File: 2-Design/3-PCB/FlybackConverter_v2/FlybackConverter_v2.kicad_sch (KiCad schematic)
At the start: 55 parts, among them U1 TL431DBZ, U2 LM7812_TO220

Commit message: Gate loop is not long anymore. Still, why not be sad :(.
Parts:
- CA1: value C -> 1n
- CF1: value C -> 20p
- CP1: value C -> NAN
- CS1: value C -> 10n
- CSnubber1: value C -> 4.7u-2220-50V
- CT1: value C -> 0.72n
- CZ1: value C -> 20n
- DSnubber1: value MBRA340 -> M3/5BT; footprint Diode_SMD:D_SMA -> Diode_SMD:D_SMB_Handsoldering
- FLYBACK_DIODE_SUBSTITUTE1: footprint Diode_SMD:D_SMC -> Diode_SMD:D_SMC_Handsoldering
- RA1, RF1, RJ1, RP1: value R -> 10k
- RAC1, RE1: value R -> 1k
- RB1, RC1, RK1: value R -> 4.7k
- RCS1: value R -> 10m
- RG1: value R -> 10
- RG2, RZ1: value R -> 22k
- RI1: value R -> 85k
- RS1: value R -> 330k
- RS2: value R -> 2.2k
- RSnubber1: value R -> 82//82
- RT1: value 10 -> 12k
- renumbered DC1 to D_Z_10V1, TVS1 to D_Z_15V1
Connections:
- net GND: now also RG2.1
- net at MOSFET1.1 (S), RCS1.1, RS2.2: no longer RG2.1
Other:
- moved on the sheet: RA1

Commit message: [PCB] board update
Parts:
- added CSnubber2: 4.7u-2220-50V, Capacitor_SMD:C_1210_3225Metric_Pad1.33x2.70mm_HandSolder, symbol Device:C
- added RG3: 0, Resistor_SMD:R_1206_3216Metric, symbol Device:R
- added RSnubber2: 82//82, Resistor_SMD:R_2010_5025Metric_Pad1.40x2.65mm_HandSolder, symbol Device:R
- CF1: value 20p -> 22p
- CZ1: value 20n -> 22n
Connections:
- net at CIN1.1, CIN2.1, CIN3.1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: now also CSnubber2.1, RG3.2, RSnubber2.1; no longer U2.1 (VI)
- net at CSnubber1.2, DSnubber1.1 (K), RSnubber1.2: now also CSnubber2.2, RSnubber2.2
- new net: RG3.1, U2.1 (VI)
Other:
- note added: "TO DO - heatsink model [DONE] - transformer model[DONE] - connector size check [DONE] - optpcoupler freq check [DONE] - current sense check (sim, iranian resistor) [DONE] - components layer check [DONE] - via check [DONE] - plexi case"
- note removed: "TO DO - heatsink model - transformer model - connector size check - optpcoupler freq check - current sense check (sim, iranian resistor) - components layer check - via check - plexi case"
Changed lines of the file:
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@@
 (kicad_sch (version 20211123) (generator eeschema)
   (paper "A4")
+  (junction (at 173.99 38.1) (diameter 0) (color 0 0 0 0)
+  )
   (junction (at 100.33 72.39) (diameter 0) (color 0 0 0 0)
   )
@@
   (junction (at 105.41 38.1) (diameter 0) (color 0 0 0 0)
   )
+  (junction (at 171.45 49.53) (diameter 0) (color 0 0 0 0)
+  )
   (junction (at 154.94 128.27) (diameter 0) (color 0 0 0 0)
   )
@@
   (junction (at 180.34 86.36) (diameter 0) (color 0 0 0 0)
   )
+  (junction (at 171.45 38.1) (diameter 0) (color 0 0 0 0)
+  )
   (junction (at 87.63 62.23) (diameter 0) (color 0 0 0 0)
   )
@@
   (junction (at 224.79 44.45) (diameter 0) (color 0 0 0 0)
   )
+  (junction (at 173.99 49.53) (diameter 0) (color 0 0 0 0)
+  )
   (junction (at 97.79 74.93) (diameter 0) (color 0 0 0 0)
   )
@@
   (junction (at 64.77 62.23) (diameter 0) (color 0 0 0 0)
   )
-  (wire (pts (xy 147.32 57.15) (xy 161.29 57.15))
+  (wire (pts (xy 147.32 57.15) (xy 148.59 57.15))
     (stroke (width 0) (type default) (color 0 0 0 0))
   )
@@
     (stroke (width 0) (type default) (color 0 0 0 0))
   )
+  (wire (pts (xy 156.21 57.15) (xy 161.29 57.15))
+    (stroke (width 0) (type default) (color 0 0 0 0))
+  )
   (wire (pts (xy 115.57 55.88) (xy 129.54 55.88))
     (stroke (width 0) (type default) (color 0 0 0 0))
@@
     (stroke (width 0) (type default) (color 0 0 0 0))
   )
+  (wire (pts (xy 171.45 38.1) (xy 171.45 40.64))
+    (stroke (width 0) (type default) (color 0 0 0 0))
+  )
   (wire (pts (xy 172.72 86.36) (xy 180.34 86.36))
     (stroke (width 0) (type default) (color 0 0 0 0))
   )
+  (wire (pts (xy 173.99 49.53) (xy 171.45 49.53))
+    (stroke (width 0) (type default) (color 0 0 0 0))
+  )
   (wire (pts (xy 153.67 87.63) (xy 153.67 88.9))
     (stroke (width 0) (type default) (color 0 0 0 0))
@@
     (stroke (width 0) (type default) (color 0 0 0 0))
   )
-  (wire (pts (xy 176.53 49.53) (xy 170.18 49.53))
+  (wire (pts (xy 176.53 49.53) (xy 173.99 49.53))
     (stroke (width 0) (type default) (color 0 0 0 0))
   )
@@
     (stroke (width 0) (type default) (color 0 0 0 0))
   )
+  (wire (pts (xy 173.99 38.1) (xy 173.99 40.64))
+    (stroke (width 0) (type default) (color 0 0 0 0))
+  )
   (wire (pts (xy 147.32 116.84) (xy 147.32 111.76))
     (stroke (width 0) (type default) (color 0 0 0 0))
@@
     (stroke (width 0) (type default) (color 0 0 0 0))
   )
+  (wire (pts (xy 173.99 38.1) (xy 176.53 38.1))
+    (stroke (width 0) (type default) (color 0 0 0 0))
+  )
+  (wire (pts (xy 171.45 49.53) (xy 170.18 49.53))
+    (stroke (width 0) (type default) (color 0 0 0 0))
+  )
   (wire (pts (xy 167.64 60.96) (xy 167.64 78.74))
     (stroke (width 0) (type default) (color 0 0 0 0))
@@
     (stroke (width 0) (type default) (color 0 0 0 0))
   )
+  (wire (pts (xy 171.45 48.26) (xy 171.45 49.53))
+    (stroke (width 0) (type default) (color 0 0 0 0))
+  )
+  (wire (pts (xy 173.99 48.26) (xy 173.99 49.53))
+    (stroke (width 0) (type default) (color 0 0 0 0))
+  )
   (wire (pts (xy 176.53 48.26) (xy 176.53 49.53))
     (stroke (width 0) (type default) (color 0 0 0 0))
@@
     (stroke (width 0) (type default) (color 0 0 0 0))
   )
-  (wire (pts (xy 166.37 38.1) (xy 176.53 38.1))
+  (wire (pts (xy 166.37 38.1) (xy 171.45 38.1))
     (stroke (width 0) (type default) (color 0 0 0 0))
   )
@@
     (stroke (width 0) (type default) (color 0 0 0 0))
   )
+  (wire (pts (xy 171.45 38.1) (xy 173.99 38.1))
+    (stroke (width 0) (type default) (color 0 0 0 0))
+  )
   (wire (pts (xy 165.1 64.77) (xy 172.72 64.77))
     (stroke (width 0) (type default) (color 0 0 0 0))
@@
     (stroke (width 0) (type default) (color 0 0 0 0))
   )
-  (text "TO DO\n- heatsink model\n- transformer model\n- connector size check\n- optpcoupler freq check\n- current sense check (sim, iranian resistor)\n- components layer check\n- via check\n- plexi case\n"
+  (text "TO DO\n- heatsink model [DONE]\n- transformer model[DONE]\n- connector size check [DONE]\n- optpcoupler freq check [DONE]\n- current sense check (sim, iranian resistor) [DONE]\n- components layer check [DONE]\n- via check [DONE]\n- plexi case\n"
     (at 13.97 34.29 0)
     (effects (font (size 1.27 1.27)) (justify left bottom))
@@
     (pin "1")
   )
+  (symbol (lib_id "Device:R") (at 152.4 57.15 90) (unit 1)
+    (in_bom yes) (on_board yes)
+    (property "Reference" "RG3" (id 0) (at 152.4 52.07 90))
+    (property "Value" "0" (id 1) (at 152.4 54.61 90))
+    (property "Footprint" "Resistor_SMD:R_1206_3216Metric" (id 2) (at 152.4 58.928 90)
+      (effects (font (size 1.27 1.27)) hide)
+    )
+    (property "Datasheet" "~" (id 3) (at 152.4 57.15 0)
+      (effects (font (size 1.27 1.27)) hide)
+    )
+    (pin "1")
+    (pin "2")
+  )
   (symbol (lib_id "Device:C") (at 76.2 55.88 90) (unit 1)
     (in_bom yes) (on_board yes)
@@
     (in_bom yes) (on_board yes)
     (property "Reference" "CZ1" (id 0) (at 170.18 116.84 90))
-    (property "Value" "20n" (id 1) (at 170.18 119.38 90))
+    (property "Value" "22n" (id 1) (at 170.18 119.38 90))
     (property "Footprint" "Capacitor_SMD:C_0805_2012Metric_Pad1.18x1.45mm_HandSolder" (id 2) (at 173.99 122.2248 0)
       (effects (font (size 1.27 1.27)) hide)
@@
     (pin "2")
   )
+  (symbol (lib_id "Device:R") (at 173.99 44.45 0) (unit 1)
+    (in_bom yes) (on_board yes)
+    (property "Reference" "RSnubber2" (id 0) (at 171.45 34.29 0)
+      (effects (font (size 1.27 1.27)) (justify left))
+    )
+    (property "Value" "82//82" (id 1) (at 172.72 36.83 0)
+      (effects (font (size 1.27 1.27)) (justify left))
+    )
+    (property "Footprint" "Resistor_SMD:R_2010_5025Metric_Pad1.40x2.65mm_HandSolder" (id 2) (at 172.212 44.45 90)
+      (effects (font (size 1.27 1.27)) hide)
+    )
+    (property "Datasheet" "~" (id 3) (at 173.99 44.45 0)
+      (effects (font (size 1.27 1.27)) hide)
+    )
+    (pin "1")
+    (pin "2")
+  )
   (symbol (lib_id "Reference_Voltage:TL431DBZ") (at 147.32 128.27 270) (mirror x) (unit 1)
     (in_bom yes) (on_board yes) (fields_autoplaced)
@@
       (effects (font (size 1.27 1.27)) (justify left))
     )
-    (property "Value" "20p" (id 1) (at 157.48 81.2799 0)
+    (property "Value" "22p" (id 1) (at 157.48 81.2799 0)
       (effects (font (size 1.27 1.27)) (justify left))
     )
@@
     (pin "2")
   )
+  (symbol (lib_id "Device:C") (at 171.45 44.45 0) (unit 1)
+    (in_bom yes) (on_board yes)
+    (property "Reference" "CSnubber2" (id 0) (at 166.37 34.29 0)
+      (effects (font (size 1.27 1.27)) (justify left))
+    )
+    (property "Value" "4.7u-2220-50V" (id 1) (at 163.83 36.83 0)
+      (effects (font (size 1.27 1.27)) (justify left))
+    )
+    (property "Footprint" "Capacitor_SMD:C_1210_3225Metric_Pad1.33x2.70mm_HandSolder" (id 2) (at 172.4152 48.26 0)
+      (effects (font (size 1.27 1.27)) hide)
+    )
+    (property "Datasheet" "~" (id 3) (at 171.45 44.45 0)
+      (effects (font (size 1.27 1.27)) hide)
+    )
+    (pin "1")
+    (pin "2")
+  )
   (symbol (lib_id "power:GND") (at 77.47 88.9 0) (unit 1)
     (in_bom yes) (on_board yes) (fields_autoplaced)
@@
     )
     (path "/da100607-de9d-46da-82db-5654a279cf3a"
-      (reference "CF1") (unit 1) (value "20p") (footprint "Capacitor_SMD:C_0805_2012Metric_Pad1.18x1.45mm_HandSolder")
+      (reference "CF1") (unit 1) (value "22p") (footprint "Capacitor_SMD:C_0805_2012Metric_Pad1.18x1.45mm_HandSolder")
     )
     (path "/89fb83e8-7ef8-4b01-a678-60ce797e61a3"
@@
       (reference "CSnubber1") (unit 1) (value "4.7u-2220-50V") (footprint "Capacitor_SMD:C_1210_3225Metric_Pad1.33x2.70mm_HandSolder")
     )
+    (path "/facf4754-2004-4a19-8c5b-1214bc491e2e"
+      (reference "CSnubber2") (unit 1) (value "4.7u-2220-50V") (footprint "Capacitor_SMD:C_1210_3225Metric_Pad1.33x2.70mm_HandSolder")
+    )
     (path "/54de77c6-37ae-452a-88ca-f7c5ad6560f1"
       (reference "CT1") (unit 1) (value "0.72n") (footprint "Capacitor_SMD:C_0805_2012Metric_Pad1.18x1.45mm_HandSolder")
@@
     )
     (path "/3552d5d9-3393-4e44-b549-ad7dcaf47867"
-      (reference "CZ1") (unit 1) (value "20n") (footprint "Capacitor_SMD:C_0805_2012Metric_Pad1.18x1.45mm_HandSolder")
+      (reference "CZ1") (unit 1) (value "22n") (footprint "Capacitor_SMD:C_0805_2012Metric_Pad1.18x1.45mm_HandSolder")
     )
     (path "/e6040600-fa22-41e1-a300-9b6e6350445e"
@@
       (reference "RG2") (unit 1) (value "22k") (footprint "Resistor_SMD:R_0805_2012Metric_Pad1.20x1.40mm_HandSolder")
     )
+    (path "/2f66bccd-5f6b-4add-9fa1-a8205592fa9b"
+      (reference "RG3") (unit 1) (value "0") (footprint "Resistor_SMD:R_1206_3216Metric")
+    )
     (path "/437ea7de-cd77-46c4-b2c8-e28e90a5651d"
       (reference "RI1") (unit 1) (value "85k") (footprint "Resistor_SMD:R_0805_2012Metric_Pad1.20x1.40mm_HandSolder")
@@
       (reference "RSnubber1") (unit 1) (value "82//82") (footprint "Resistor_SMD:R_2010_5025Metric_Pad1.40x2.65mm_HandSolder")
     )
+    (path "/b1698430-659f-4b80-a575-c7b731e4c2e7"
+      (reference "RSnubber2") (unit 1) (value "82//82") (footprint "Resistor_SMD:R_2010_5025Metric_Pad1.40x2.65mm_HandSolder")
+    )
     (path "/5fb96c6a-ab0f-446b-92fa-b00a4a51357b"

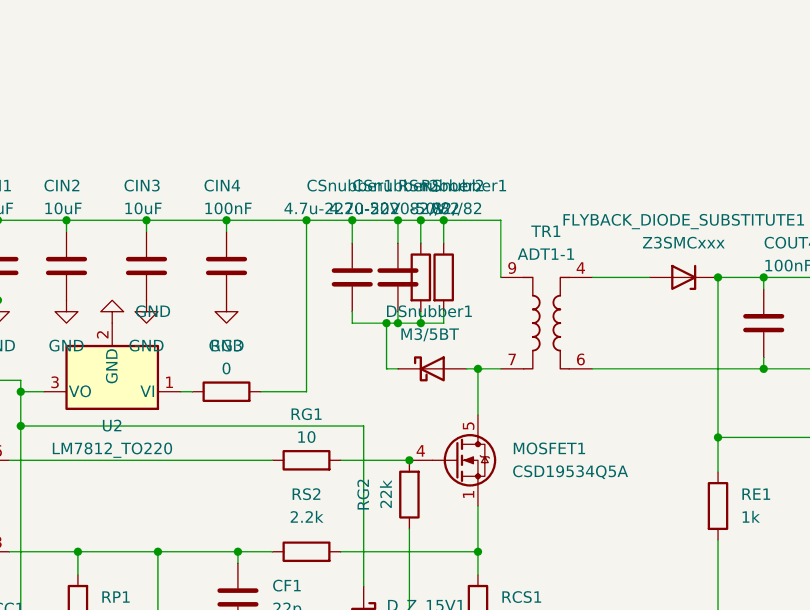
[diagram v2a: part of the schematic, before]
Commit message: [PCB] snubber resistor change
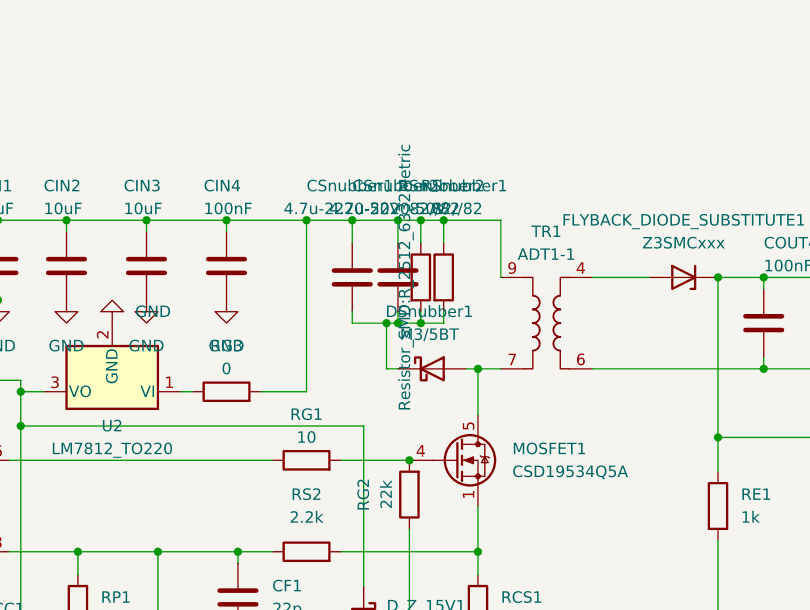
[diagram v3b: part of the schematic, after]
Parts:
- DSnubber1: footprint Diode_SMD:D_SMB_Handsoldering -> Diode_SMD:D_SMB
- RSnubber1, RSnubber2: footprint Resistor_SMD:R_2010_5025Metric_Pad1.40x2.65mm_HandSolder -> Resistor_SMD:R_2512_6332Metric
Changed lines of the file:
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@@
       (effects (font (size 1.27 1.27)) (justify left))
     )
-    (property "Footprint" "Resistor_SMD:R_2010_5025Metric_Pad1.40x2.65mm_HandSolder" (id 2) (at 172.212 44.45 90)
-      (effects (font (size 1.27 1.27)) hide)
-    )
+    (property "Footprint" "Resistor_SMD:R_2512_6332Metric" (id 2) (at 172.212 44.45 90))
     (property "Datasheet" "~" (id 3) (at 173.99 44.45 0)
       (effects (font (size 1.27 1.27)) hide)
@@
       (effects (font (size 1.27 1.27)) (justify left))
     )
-    (property "Footprint" "Resistor_SMD:R_2010_5025Metric_Pad1.40x2.65mm_HandSolder" (id 2) (at 174.752 44.45 90)
+    (property "Footprint" "Resistor_SMD:R_2512_6332Metric" (id 2) (at 174.752 44.45 90)
       (effects (font (size 1.27 1.27)) hide)
     )
@@
     (property "Reference" "DSnubber1" (id 0) (at 174.9425 48.26 0))
     (property "Value" "M3/5BT" (id 1) (at 174.9425 50.8 0))
-    (property "Footprint" "Diode_SMD:D_SMB_Handsoldering" (id 2) (at 175.26 59.055 0)
+    (property "Footprint" "Diode_SMD:D_SMB" (id 2) (at 175.26 59.055 0)
       (effects (font (size 1.27 1.27)) hide)
     )
@@
     )
     (path "/e6040600-fa22-41e1-a300-9b6e6350445e"
-      (reference "DSnubber1") (unit 1) (value "M3/5BT") (footprint "Diode_SMD:D_SMB_Handsoldering")
+      (reference "DSnubber1") (unit 1) (value "M3/5BT") (footprint "Diode_SMD:D_SMB")
     )
     (path "/14c7ef54-cc8d-4e3a-aea4-32382626f4f7"
@@
     )
     (path "/ca23ebe5-09af-4b93-8bd5-5f14974a31b1"
-      (reference "RSnubber1") (unit 1) (value "82//82") (footprint "Resistor_SMD:R_2010_5025Metric_Pad1.40x2.65mm_HandSolder")
+      (reference "RSnubber1") (unit 1) (value "82//82") (footprint "Resistor_SMD:R_2512_6332Metric")
     )
     (path "/b1698430-659f-4b80-a575-c7b731e4c2e7"
-      (reference "RSnubber2") (unit 1) (value "82//82") (footprint "Resistor_SMD:R_2010_5025Metric_Pad1.40x2.65mm_HandSolder")
+      (reference "RSnubber2") (unit 1) (value "82//82") (footprint "Resistor_SMD:R_2512_6332Metric")
     )
     (path "/5fb96c6a-ab0f-446b-92fa-b00a4a51357b"

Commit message: [PCB] last corrections and cillibom
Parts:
- added COUT5: 100nF, Capacitor_SMD:C_1206_3216Metric, symbol Device:C
- added RES1: 1k, Resistor_SMD:R_2512_6332Metric, symbol Device:R
- FLYBACK_DIODE_SUBSTITUTE1: footprint Diode_SMD:D_SMC_Handsoldering -> Diode_SMD:D_SMC
- RE1: value 1k -> 2.2k
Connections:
- net at COUT1.1, COUT2.1, COUT3.1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: now also COUT5.2
- net at FLYBACK_DIODE_SUBSTITUTE1.2 (A), TR1.4 (w~): now also RES1.1
- new net: COUT5.1, RES1.2
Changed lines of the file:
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@@
   (junction (at 153.67 74.93) (diameter 0) (color 0 0 0 0)
   )
+  (junction (at 214.63 44.45) (diameter 0) (color 0 0 0 0)
+  )
   (junction (at 219.71 62.23) (diameter 0) (color 0 0 0 0)
   )
@@
   (junction (at 147.32 123.19) (diameter 0) (color 0 0 0 0)
   )
+  (junction (at 195.58 44.45) (diameter 0) (color 0 0 0 0)
+  )
   (junction (at 99.06 116.84) (diameter 0) (color 0 0 0 0)
   )
@@
     (stroke (width 0) (type default) (color 0 0 0 0))
   )
+  (wire (pts (xy 214.63 33.02) (xy 214.63 44.45))
+    (stroke (width 0) (type default) (color 0 0 0 0))
+  )
   (wire (pts (xy 207.01 62.23) (xy 207.01 66.04))
     (stroke (width 0) (type default) (color 0 0 0 0))
@@
     (stroke (width 0) (type default) (color 0 0 0 0))
   )
+  (wire (pts (xy 212.09 33.02) (xy 214.63 33.02))
+    (stroke (width 0) (type default) (color 0 0 0 0))
+  )
   (wire (pts (xy 176.53 123.19) (xy 176.53 116.84))
     (stroke (width 0) (type default) (color 0 0 0 0))
@@
     (stroke (width 0) (type default) (color 0 0 0 0))
   )
-  (wire (pts (xy 212.09 44.45) (xy 224.79 44.45))
+  (wire (pts (xy 212.09 44.45) (xy 214.63 44.45))
     (stroke (width 0) (type default) (color 0 0 0 0))
   )
@@
     (stroke (width 0) (type default) (color 0 0 0 0))
   )
-  (wire (pts (xy 193.04 44.45) (xy 199.39 44.45))
+  (wire (pts (xy 193.04 44.45) (xy 195.58 44.45))
     (stroke (width 0) (type default) (color 0 0 0 0))
   )
@@
     (stroke (width 0) (type default) (color 0 0 0 0))
   )
+  (wire (pts (xy 214.63 44.45) (xy 224.79 44.45))
+    (stroke (width 0) (type default) (color 0 0 0 0))
+  )
   (wire (pts (xy 180.34 54.61) (xy 182.88 54.61))
     (stroke (width 0) (type default) (color 0 0 0 0))
   )
+  (wire (pts (xy 196.85 33.02) (xy 195.58 33.02))
+    (stroke (width 0) (type default) (color 0 0 0 0))
+  )
   (wire (pts (xy 102.87 64.77) (xy 87.63 64.77))
     (stroke (width 0) (type default) (color 0 0 0 0))
@@
   )
   (wire (pts (xy 153.67 74.93) (xy 153.67 76.2))
+    (stroke (width 0) (type default) (color 0 0 0 0))
+  )
+  (wire (pts (xy 195.58 44.45) (xy 199.39 44.45))
+    (stroke (width 0) (type default) (color 0 0 0 0))
+  )
+  (wire (pts (xy 195.58 33.02) (xy 195.58 44.45))
     (stroke (width 0) (type default) (color 0 0 0 0))
   )
@@
     (property "Reference" "FLYBACK_DIODE_SUBSTITUTE1" (id 0) (at 203.2 38.1 0))
     (property "Value" "Z3SMCxxx" (id 1) (at 203.2 40.64 0))
-    (property "Footprint" "Diode_SMD:D_SMC_Handsoldering" (id 2) (at 203.2 40.005 0)
+    (property "Footprint" "Diode_SMD:D_SMC" (id 2) (at 203.2 40.005 0)
       (effects (font (size 1.27 1.27)) hide)
     )
@@
     )
     (property "Datasheet" "~" (id 3) (at 161.29 74.93 0)
+      (effects (font (size 1.27 1.27)) hide)
+    )
+    (pin "1")
+    (pin "2")
+  )
+  (symbol (lib_id "Device:C") (at 208.28 33.02 90) (unit 1)
+    (in_bom yes) (on_board yes)
+    (property "Reference" "COUT5" (id 0) (at 199.39 33.02 0)
+      (effects (font (size 1.27 1.27)) (justify left))
+    )
+    (property "Value" "100nF" (id 1) (at 201.93 33.02 0)
+      (effects (font (size 1.27 1.27)) (justify left))
+    )
+    (property "Footprint" "Capacitor_SMD:C_1206_3216Metric" (id 2) (at 212.09 32.0548 0)
+      (effects (font (size 1.27 1.27)) hide)
+    )
+    (property "Datasheet" "~" (id 3) (at 208.28 33.02 0)
       (effects (font (size 1.27 1.27)) hide)
     )
@@
     (pin "3")
   )
+  (symbol (lib_id "Device:R") (at 200.66 33.02 90) (unit 1)
+    (in_bom yes) (on_board yes) (fields_autoplaced)
+    (property "Reference" "RES1" (id 0) (at 200.66 26.67 90))
+    (property "Value" "1k" (id 1) (at 200.66 29.21 90))
+    (property "Footprint" "Resistor_SMD:R_2512_6332Metric" (id 2) (at 200.66 34.798 90)
+      (effects (font (size 1.27 1.27)) hide)
+    )
+    (property "Datasheet" "~" (id 3) (at 200.66 33.02 0)
+      (effects (font (size 1.27 1.27)) hide)
+    )
+    (pin "1")
+    (pin "2")
+  )
   (symbol (lib_id "power:GND") (at 99.06 137.16 0) (unit 1)
     (in_bom yes) (on_board yes) (fields_autoplaced)
@@
       (effects (font (size 1.27 1.27)) (justify left))
     )
-    (property "Value" "1k" (id 1) (at 209.55 71.1199 0)
+    (property "Value" "2.2k" (id 1) (at 209.55 71.1199 0)
       (effects (font (size 1.27 1.27)) (justify left))
     )
@@
       (reference "COUT4") (unit 1) (value "100nF") (footprint "Capacitor_SMD:C_1210_3225Metric_Pad1.33x2.70mm_HandSolder")
     )
+    (path "/6587a352-0d84-497d-8cf7-63b0c13dbd96"
+      (reference "COUT5") (unit 1) (value "100nF") (footprint "Capacitor_SMD:C_1206_3216Metric")
+    )
     (path "/ddadd4ff-ba23-4d15-a321-847b0478405c"
       (reference "CP1") (unit 1) (value "NAN") (footprint "Capacitor_SMD:C_0805_2012Metric_Pad1.18x1.45mm_HandSolder")
@@
     )
     (path "/3e37ba8e-db34-4353-b445-c369a6553ddc"
-      (reference "FLYBACK_DIODE_SUBSTITUTE1") (unit 1) (value "Z3SMCxxx") (footprint "Diode_SMD:D_SMC_Handsoldering")
+      (reference "FLYBACK_DIODE_SUBSTITUTE1") (unit 1) (value "Z3SMCxxx") (footprint "Diode_SMD:D_SMC")
     )
     (path "/5218f09f-4a8c-4246-bbc5-dc5a647f8801"
@@
     )
     (path "/d5eca49d-042c-4463-8ab4-7c004c4938ff"
-      (reference "RE1") (unit 1) (value "1k") (footprint "Resistor_SMD:R_0805_2012Metric_Pad1.20x1.40mm_HandSolder")
+      (reference "RE1") (unit 1) (value "2.2k") (footprint "Resistor_SMD:R_0805_2012Metric_Pad1.20x1.40mm_HandSolder")
+    )
+    (path "/c2866715-a5f4-40ce-b26c-54df069380c3"
+      (reference "RES1") (unit 1) (value "1k") (footprint "Resistor_SMD:R_2512_6332Metric")
     )
     (path "/c9ca2a27-da63-447f-8ee1-46b0a936fb7d"
